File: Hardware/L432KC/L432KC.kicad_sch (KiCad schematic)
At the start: 44 parts, among them J1 L4_G4, J2 USB_B_Micro, J3 JTAG, J4 3v3, J5 GND, J6 Conn_01x07, J7 Conn_01x07_Male, J8 TVCC, J9 LogicAna, U1 AD8531ARTZ, U2 SRV05-4, U3 NUCLEO-L432KC, U4 TXB0304RUT, U5 TXB0304RUT, U6 74LVC1G125

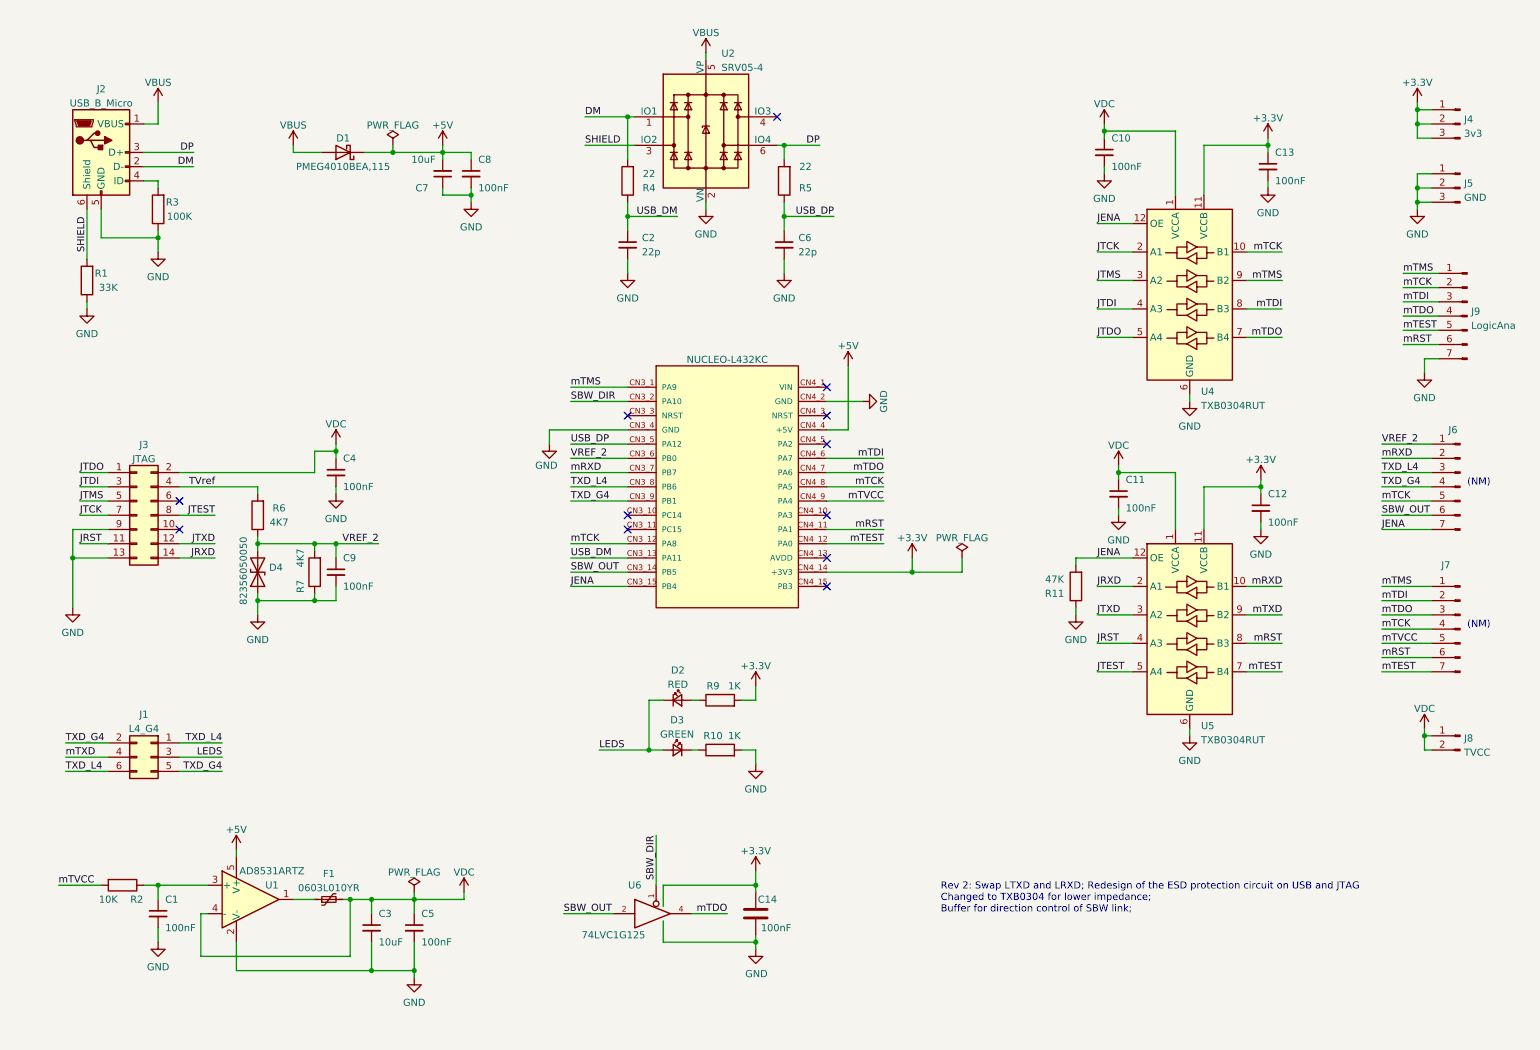
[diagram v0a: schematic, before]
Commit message: Updated L432KC/G431K6 prototype board.
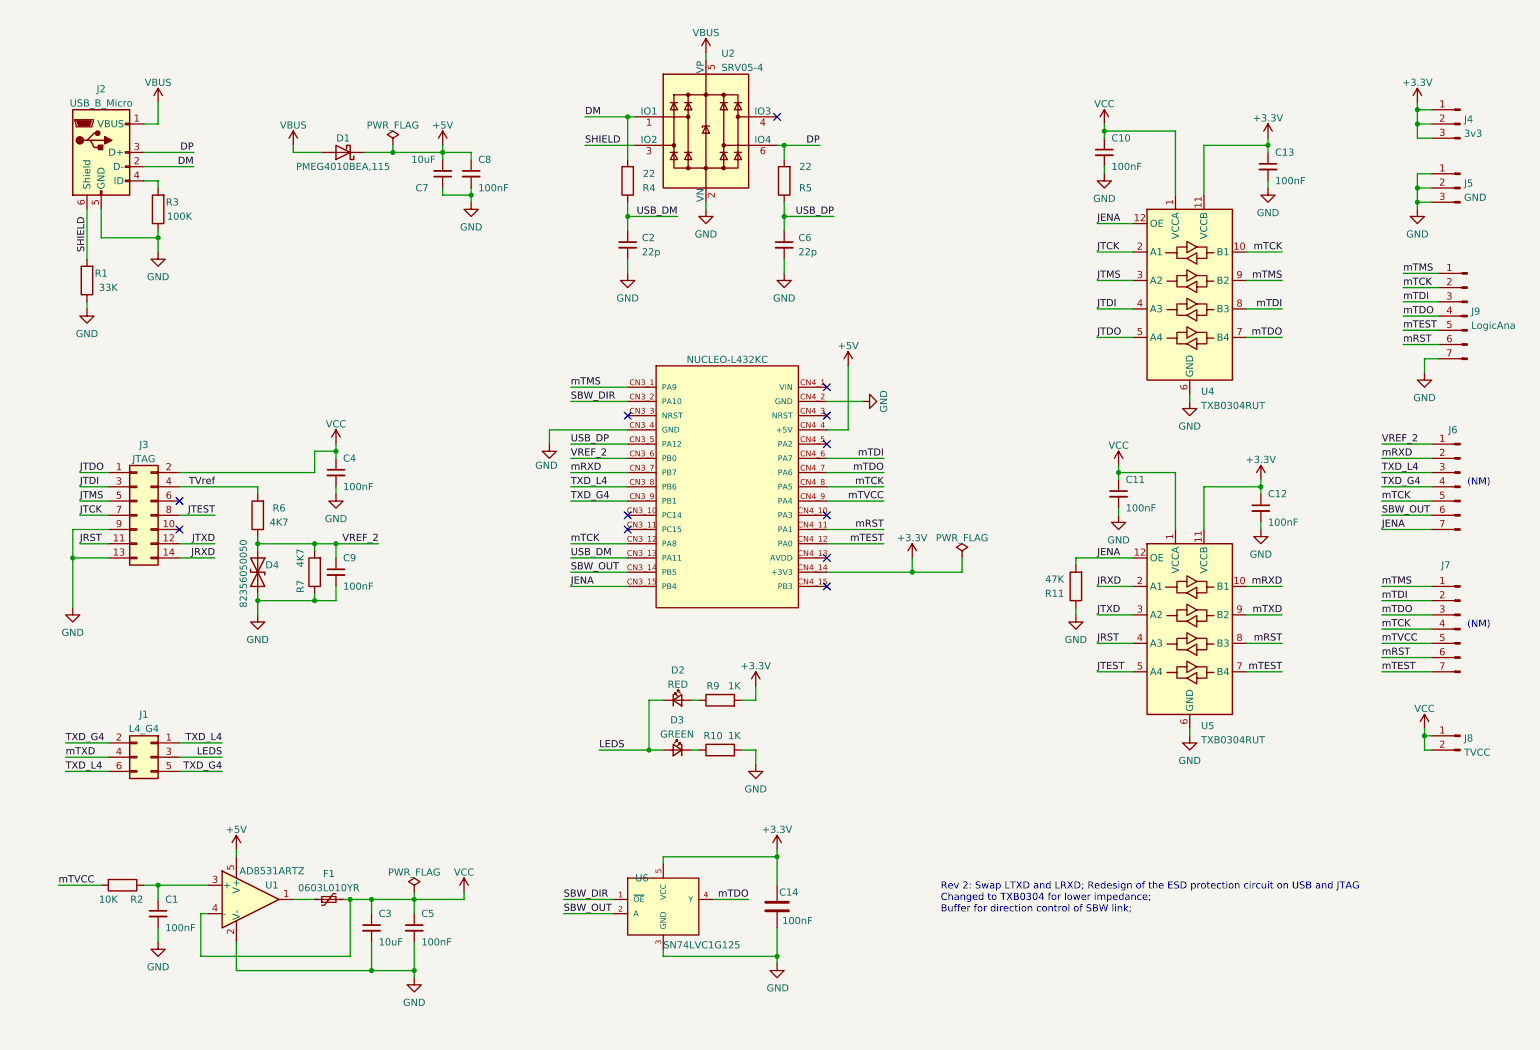
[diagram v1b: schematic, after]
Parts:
- U6: value 74LVC1G125 -> SN74LVC1G125; symbol 74xGxx:74LVC1G125 -> SN74LVC1G125:SN74LVC1G125
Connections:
- net GND: now also D4.2 (A2); no longer D4.1 (A1)
- net VREF_2: now also D4.1 (A1); no longer D4.2 (A2)
- net VDC renamed VCC
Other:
- moved on the sheet: C14, D4

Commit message: Updated L432KC prototype to use low impedance output buffers for voltage translation.
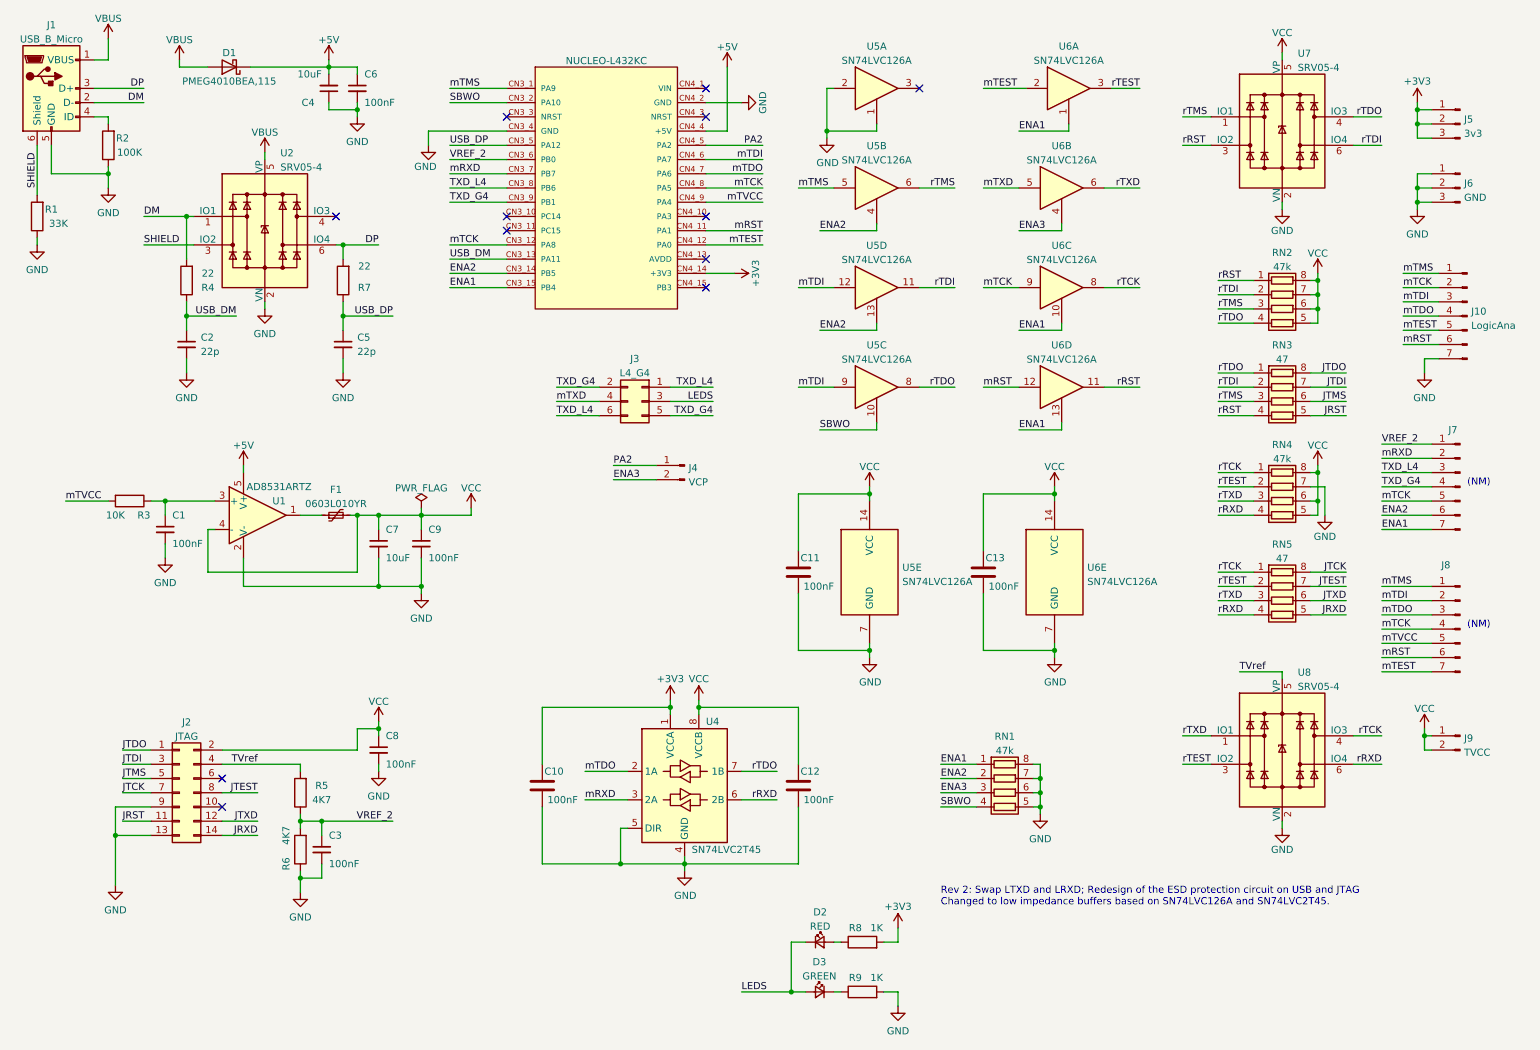
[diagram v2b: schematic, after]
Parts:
- removed C10, C11, C12, C13: 100nF, Capacitor_SMD:C_0603_1608Metric_Pad1.08x0.95mm_HandSolder, symbol Device:C_Small
- removed C14: 100nF, Capacitor_SMD:C_0603_1608Metric_Pad1.08x0.95mm_HandSolder, symbol Device:C
- removed D4: 82356050050, Diode_SMD:D_0603_1608Metric_Pad1.05x0.95mm_HandSolder, symbol Device:D_TVS
- removed R11: 47K, Resistor_SMD:R_0603_1608Metric_Pad0.98x0.95mm_HandSolder, symbol Device:R
- removed U4, U5: TXB0304RUT, Package_DFN_QFN:Texas_R_PUQFN-N12, symbol Logic_LevelTranslator:TXB0304RUT
- removed U6: SN74LVC1G125, Package_TO_SOT_SMD:SOT-23-5_HandSoldering, symbol SN74LVC1G125:SN74LVC1G125
- added C10, C11, C12, C13: 100nF, Capacitor_SMD:C_0603_1608Metric_Pad1.08x0.95mm_HandSolder, symbol Device:C
- added J4: VCP, Connector_PinHeader_2.54mm:PinHeader_1x02_P2.54mm_Vertical, symbol Connector:Conn_01x02_Male
- added RN1, RN2, RN4: 47k, Resistor_SMD:R_Array_Convex_4x0402, symbol Device:R_Pack04
- added RN3, RN5: 47, Resistor_SMD:R_Array_Convex_4x0402, symbol Device:R_Pack04
- added U4: SN74LVC2T45, Package_SO:VSSOP-8_2.3x2mm_P0.5mm, symbol Logic_LevelTranslator:74LVC2T45DC
- added U5, U6: SN74LVC126A, Package_SO:TSSOP-14_4.4x5mm_P0.65mm, symbol 74xx:74LS126
- added U7, U8: SRV05-4, Package_TO_SOT_SMD:SOT-23-6, symbol Power_Protection:SRV05-4
- U3: footprint lib:MODULE_NUCLEO-L432KC -> MODULE_NUCLEO-L432KC
- renumbered C9 to C3, C7 to C4, C6 to C5, C8 to C6, C3 to C7, C4 to C8, C5 to C9, J2 to J1, J9 to J10, J3 to J2, J1 to J3, J4 to J5, J5 to J6, J6 to J7, J7 to J8, J8 to J9, R3 to R2, R2 to R3, R6 to R5, R7 to R6, R5 to R7, R9 to R8, R10 to R9
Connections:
- net GND: now also C10.1, C11.1, C12.1, C13.1, RN1.5 (R4.2), RN1.6 (R3.2), RN1.7 (R2.2), RN1.8 (R1.2), RN4.7 (R2.2), U4.4 (GND), U4.5 (DIR), U5.1, U5.2, U5.7 (GND), U6.7 (GND), U7.2 (VN), U8.2 (VN)
- net JRST: now also RN3.5 (R4.2)
- net JRXD: now also RN5.5 (R4.2)
- net JTCK: now also RN5.8 (R1.2)
- net JTDI: now also RN3.7 (R2.2)
- net JTDO: now also RN3.8 (R1.2)
- net JTEST: now also RN5.7 (R2.2)
- net JTMS: now also RN3.6 (R3.2)
- net JTXD: now also RN5.6 (R3.2)
- net TVref: now also U8.5 (VP)
- net VCC: now also C11.2, C12.2, C13.2, RN2.5 (R4.2), RN2.6 (R3.2), RN2.7 (R2.2), RN2.8 (R1.2), RN4.5 (R4.2), RN4.6 (R3.2), RN4.8 (R1.2), U4.8 (VCCB), U5.14 (VCC), U6.14 (VCC), U7.5 (VP)
- net mRST: now also U6.12
- net mRXD: now also U4.3 (2A)
- net mTCK: now also U6.9
- net mTDI: now also U5.12, U5.9
- net mTDO: now also U4.2 (1A)
- net mTEST: now also U6.2
- net mTMS: now also U5.5
- net mTXD: now also U6.5
- net PA2: now reaches U3.CN4_5 (PA2)
- net PA2: now also J4.1 (Pin_1)
- net +3.3V renamed +3V3
- net +3V3: now also C10.2, U4.1 (VCCA)
- net JENA renamed ENA1
- net ENA1: now also RN1.1 (R1.1), U6.1, U6.10, U6.13
- net SBW_DIR renamed SBWO
- net SBWO: now also RN1.4 (R4.1), U5.10
- net SBW_OUT renamed ENA2
- net ENA2: now also RN1.2 (R2.1), U5.13, U5.4
- new net ENA3: J4.2 (Pin_2), RN1.3 (R3.1), U6.4
- new net rRST: RN2.1 (R1.1), RN3.4 (R4.1), U6.11, U7.3 (IO2)
- new net rRXD: RN4.4 (R4.1), RN5.4 (R4.1), U4.6 (2B), U8.6 (IO4)
- new net rTCK: RN4.1 (R1.1), RN5.1 (R1.1), U6.8, U8.4 (IO3)
- new net rTDI: RN2.2 (R2.1), RN3.2 (R2.1), U5.11, U7.6 (IO4)
- new net rTDO: RN2.4 (R4.1), RN3.1 (R1.1), U4.7 (1B), U5.8, U7.4 (IO3)
- new net rTEST: RN4.2 (R2.1), RN5.2 (R2.1), U6.3, U8.3 (IO2)
- new net rTMS: RN2.3 (R3.1), RN3.3 (R3.1), U5.6, U7.1 (IO1)
- new net rTXD: RN4.3 (R3.1), RN5.3 (R3.1), U6.6, U8.1 (IO1)
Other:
- note added: "Rev 2: Swap LTXD and LRXD; Redesign of the ESD protection circuit on USB and JTAG Changed to low impedance buffers based on SN74LVC126A and SN74LVC2T45."
- note removed: "Rev 2: Swap LTXD and LRXD; Redesign of the ESD protection circuit on USB and JTAG Changed to TXB0304 for lower impedance; Buffer for direction control of SBW link;"
- moved on the sheet: C1, C2, C3, C4, C5, C6, C7, C8, C9, D1, D2, D3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

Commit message: - Review of values on L432KC
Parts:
- RN3, RN5: value 47 -> 100
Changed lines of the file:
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@@
   (paper "A4")
   (title_block
-    (date "2022-11-06")
+    (date "2022-11-27")
     (rev "2")
   )
@@
     (in_bom yes) (on_board yes) (fields_autoplaced)
     (property "Reference" "RN5" (id 0) (at 240.03 108.0602 90))
-    (property "Value" "47" (id 1) (at 240.03 110.5971 90))
+    (property "Value" "100" (id 1) (at 240.03 110.5971 90))
     (property "Footprint" "Resistor_SMD:R_Array_Convex_4x0402" (id 2) (at 240.03 125.095 90)
       (effects (font (size 1.27 1.27)) hide)
@@
     (in_bom yes) (on_board yes) (fields_autoplaced)
     (property "Reference" "RN3" (id 0) (at 240.03 72.5002 90))
-    (property "Value" "47" (id 1) (at 240.03 75.0371 90))
+    (property "Value" "100" (id 1) (at 240.03 75.0371 90))
     (property "Footprint" "Resistor_SMD:R_Array_Convex_4x0402" (id 2) (at 240.03 89.535 90)
       (effects (font (size 1.27 1.27)) hide)
@@
     )
     (path "/f5ecb74b-1891-426f-8125-6376af3a4ac5"
-      (reference "RN3") (unit 1) (value "47") (footprint "Resistor_SMD:R_Array_Convex_4x0402")
+      (reference "RN3") (unit 1) (value "100") (footprint "Resistor_SMD:R_Array_Convex_4x0402")
     )
     (path "/1f05f679-b94b-4bb1-b73f-3ba3b2bce454"
@@
     )
     (path "/48ffd139-4bf7-4313-af62-1cf7d3637d31"
-      (reference "RN5") (unit 1) (value "47") (footprint "Resistor_SMD:R_Array_Convex_4x0402")
+      (reference "RN5") (unit 1) (value "100") (footprint "Resistor_SMD:R_Array_Convex_4x0402")
     )
     (path "/5b064358-fc93-4228-9d9a-2a54412eda1e"

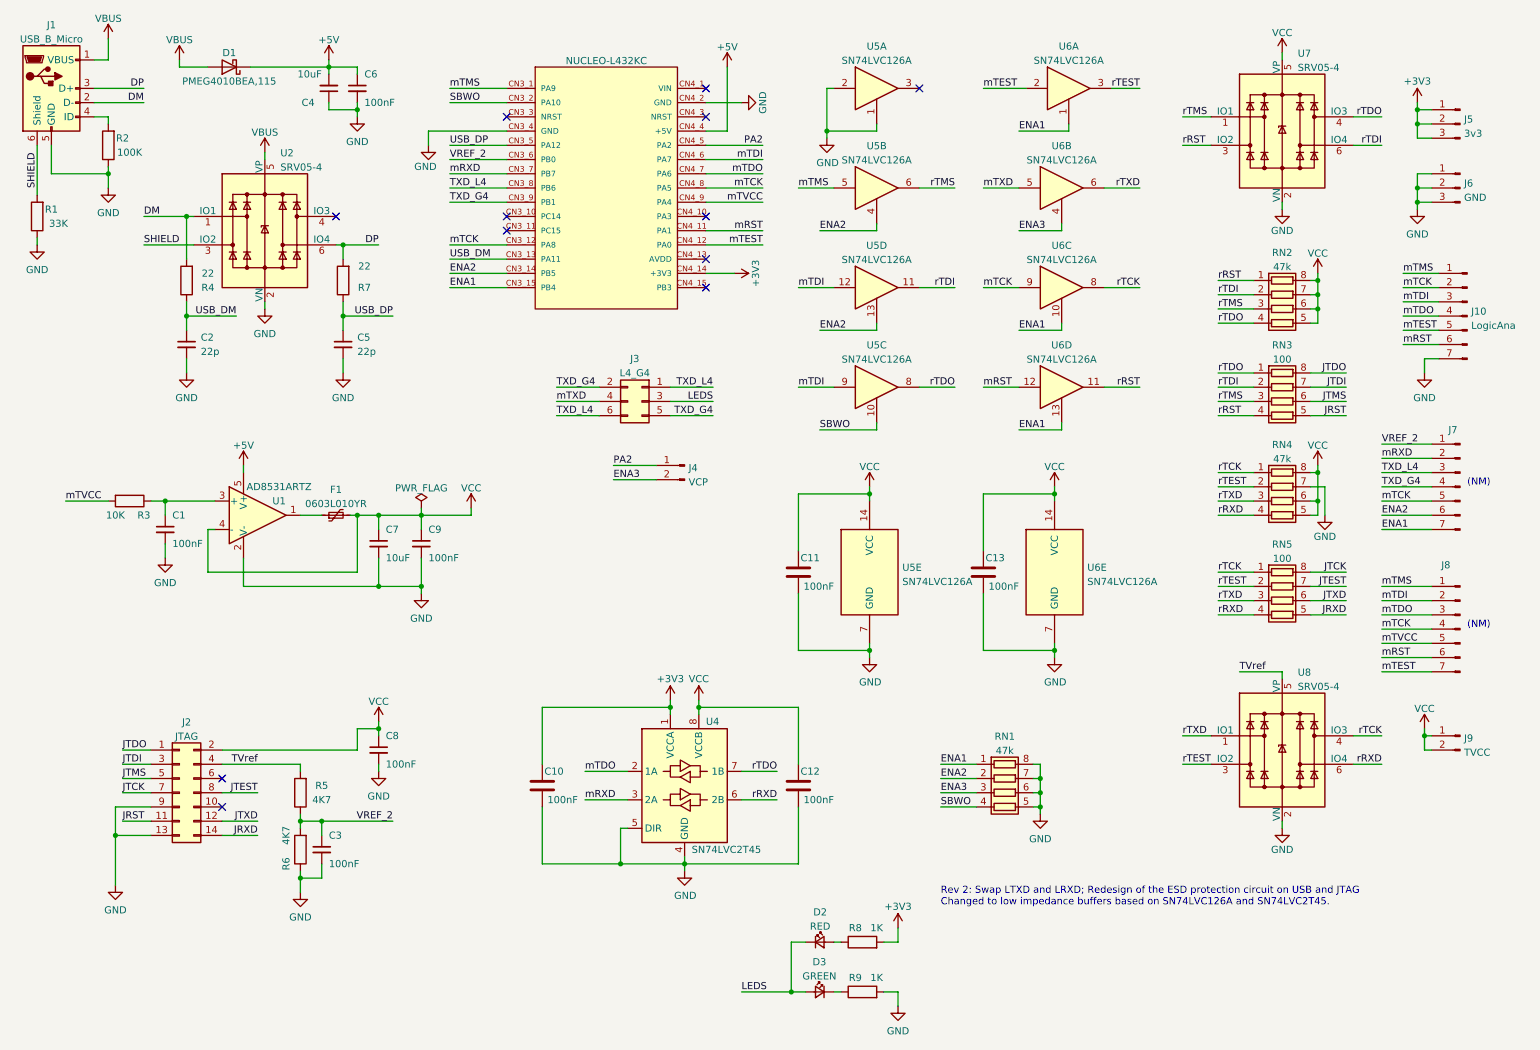
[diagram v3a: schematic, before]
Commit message: Changed output buffer part#
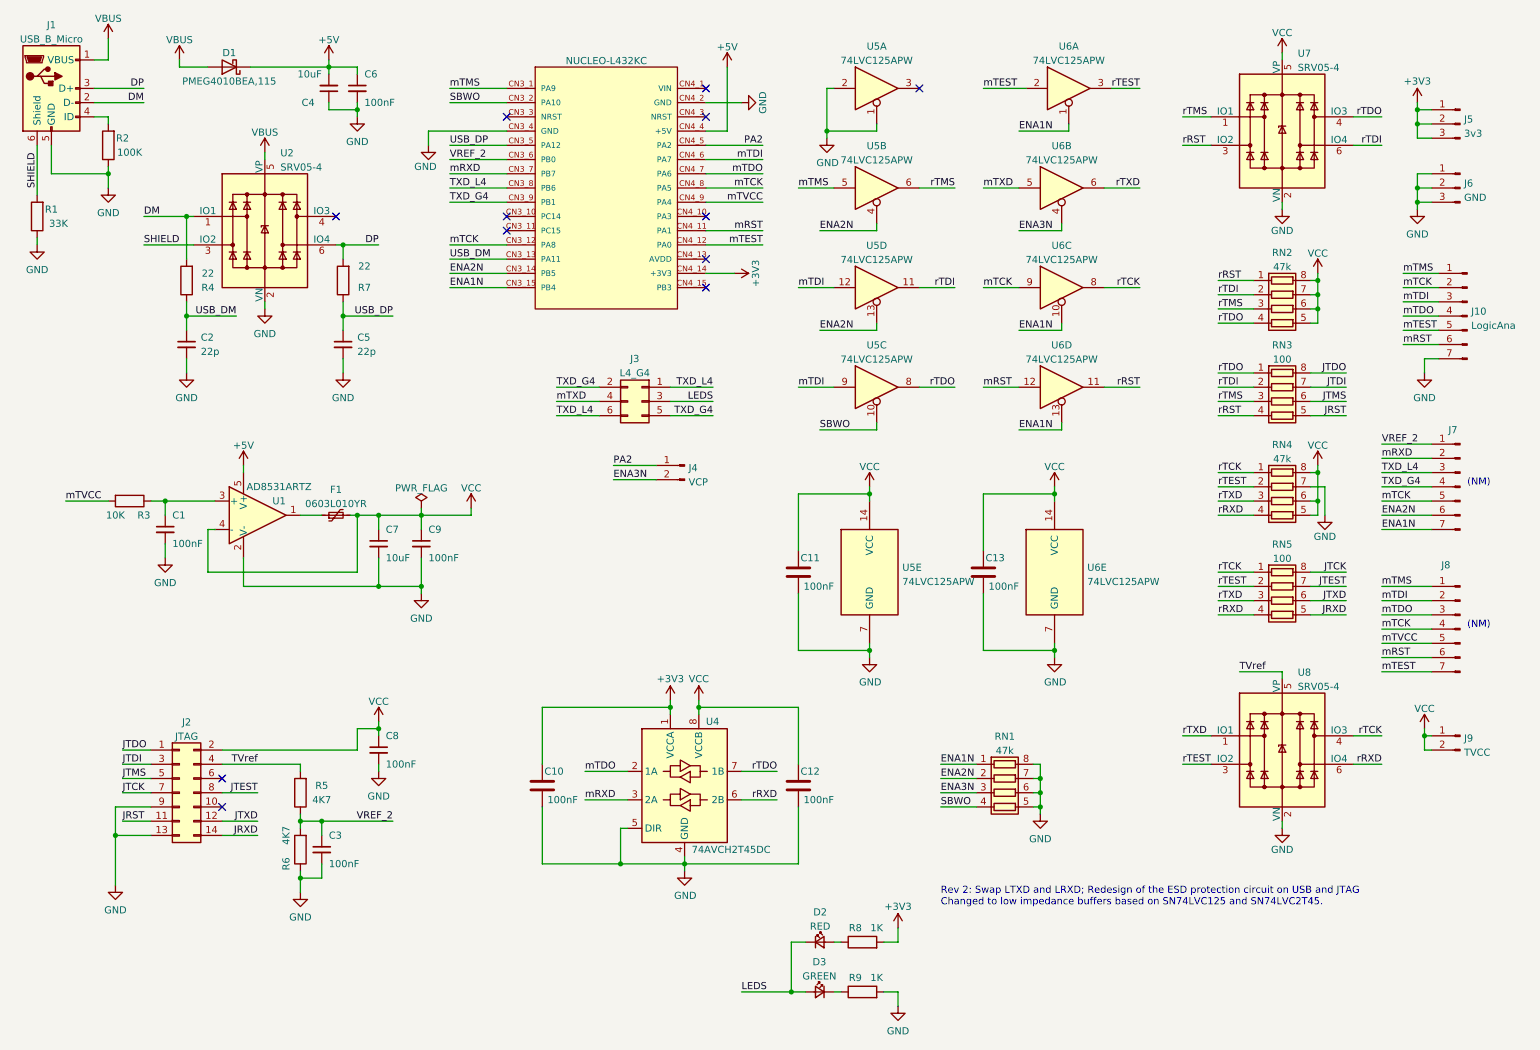
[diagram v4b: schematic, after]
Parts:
- U4: value SN74LVC2T45 -> 74AVCH2T45DC
- U5, U6: value SN74LVC126A -> 74LVC125APW; symbol 74xx:74LS126 -> 74xx:74LS125
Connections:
- net ENA1 renamed ENA1N
- net ENA2 renamed ENA2N
- net ENA3 renamed ENA3N
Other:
- note added: "Rev 2: Swap LTXD and LRXD; Redesign of the ESD protection circuit on USB and JTAG Changed to low impedance buffers based on SN74LVC125 and SN74LVC2T45."
- note removed: "Rev 2: Swap LTXD and LRXD; Redesign of the ESD protection circuit on USB and JTAG Changed to low impedance buffers based on SN74LVC126A and SN74LVC2T45."
